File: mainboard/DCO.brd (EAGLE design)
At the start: 59.4 x 23 mm, 45 parts, among them IC101 LF353D, IC201 LF353D, P101 TRIMPOT 100K, U1 XMEGA-A4VQFN

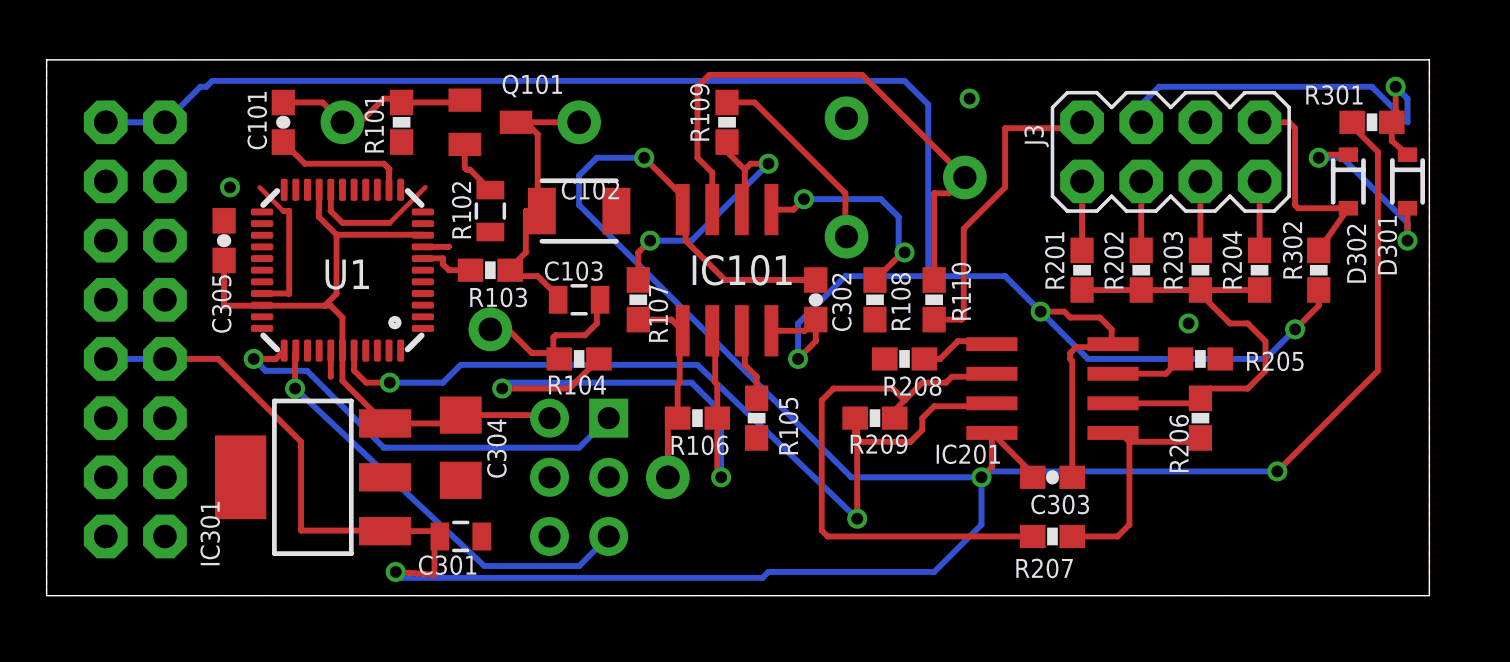
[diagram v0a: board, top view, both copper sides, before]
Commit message: rerouted, switched to TQFP xmega
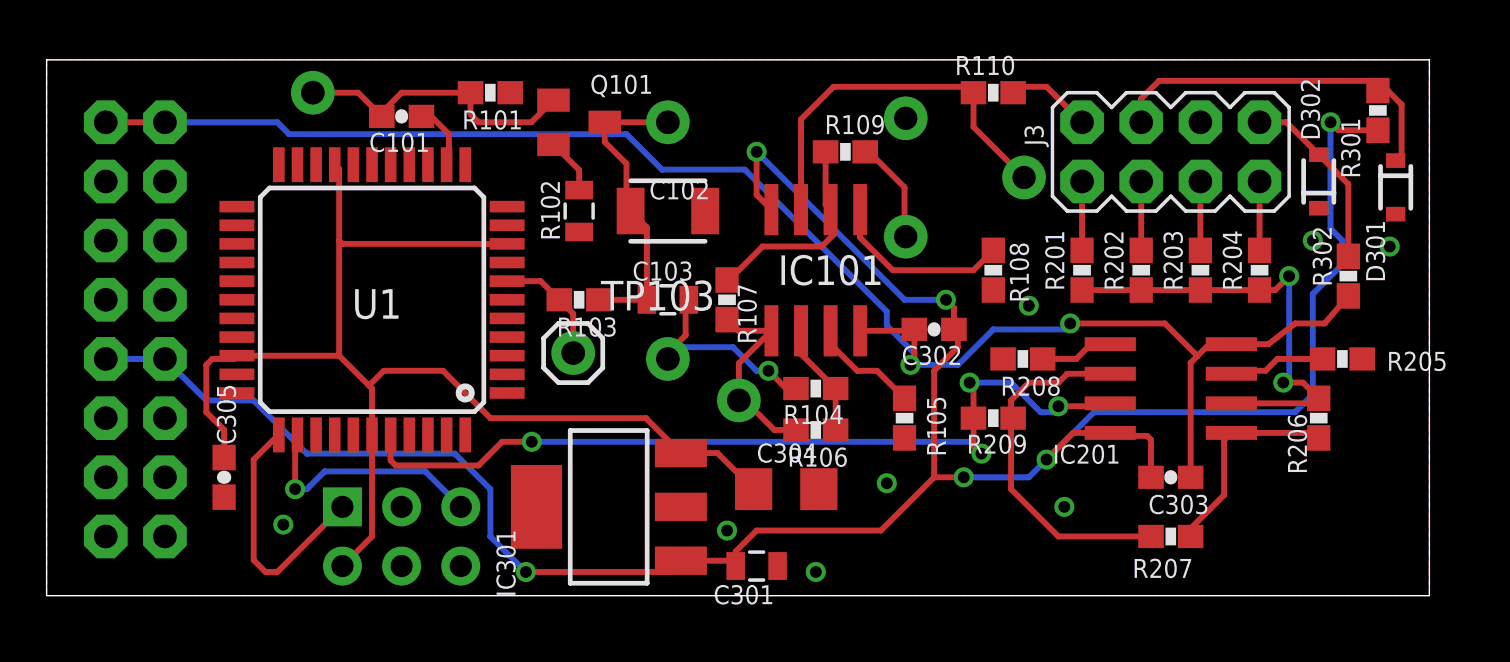
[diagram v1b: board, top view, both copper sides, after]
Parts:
- added TP105: (no value), SparkFun:1X01
- R102: value 3.9 -> 1
- U1: value XMEGA-A4VQFN -> XMEGA-A4TQFP; device custom:QFN44 -> avr-7:TQFP44
- moved C304 14.1 mm to (31.8, 4.57), turned to 0 degrees
- moved C301 12.8 mm to (30.5, 1.27)
- moved IC301 12.8 mm to (24.1, 3.81)
- moved R104 10.2 mm to (33.0, 8.89)
- moved C305 10.2 mm to (7.62, 5.08), turned to 90 degrees
- moved R110 9.25 mm to (40.6, 21.6), turned to 0 degrees
- moved H1 8.03 mm to (15.2, 2.54), turned to 270 degrees
- moved R105 6.35 mm to (36.8, 7.62)
- moved R205 6.10 mm to (55.6, 10.2)
- moved C302 5.24 mm to (38.1, 11.4), turned to 0 degrees
- moved R108 5.24 mm to (40.6, 14.0)
- moved R109 5.24 mm to (34.3, 19.1), turned to 0 degrees
- moved R106 5.11 mm to (33.0, 7.11)
- moved C101 5.09 mm to (15.2, 20.6), turned to 0 degrees
- moved TP104 5.08 mm to (26.7, 10.2)
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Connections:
- net FREQCV: now also TP103.1
- net N$13: now also TP105.1; no longer TP104.1
- net N$5: now also TP104.1; no longer TP103.1
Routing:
- net +3V3: track 29.0 -> 54.7 mm
- net GND: track 22.8 -> 0.00 mm, vias 5 -> 8
- net +12V: track 123.5 -> 103.5 mm, vias 4 -> 6
- net R104: track 23.9 -> 4.87 mm, vias 2 -> 0
- net -12V: track 87.5 -> 70.2 mm, vias 3 -> 2
- net OUT: track 13.6 -> 3.70 mm
- net N$19: track 23.9 -> 15.5 mm
- net RESET: track 18.6 -> 10.4 mm
- net N$11: track 24.4 -> 16.5 mm
- net PDI_DATA: track 18.8 -> 11.0 mm, vias 1 -> 0
- net N$12: track 8.58 -> 4.46 mm
- net N$2: track 8.67 -> 12.7 mm
- net N$3: track 12.7 -> 9.07 mm, vias 2 -> 0
- net FREQ: track 5.96 -> 2.85 mm
- net FREQCV: track 2.41 -> 5.10 mm
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
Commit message: edited labels
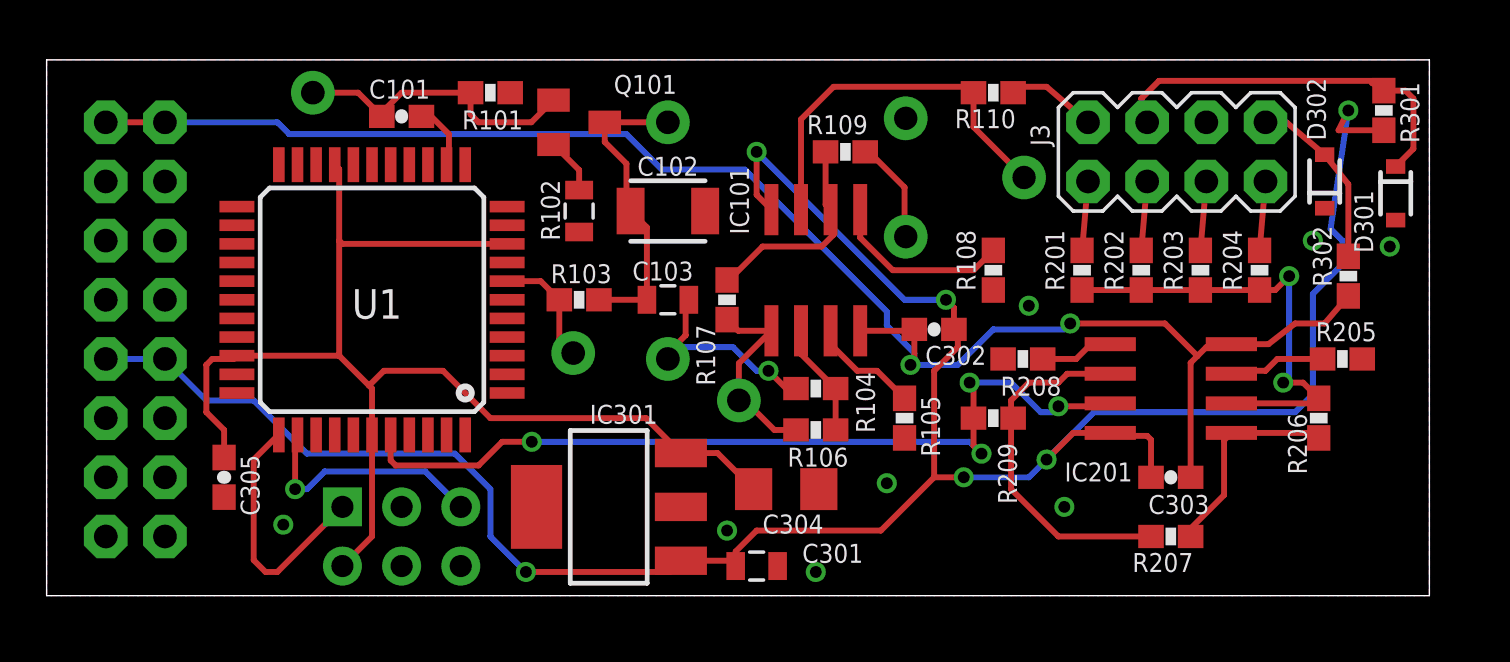
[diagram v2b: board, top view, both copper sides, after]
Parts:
- moved U$1 40.7 mm to (15.0, 15.2)
- moved J3 0.25 mm to (48.5, 19.1)
- moved R301 0.25 mm to (57.4, 20.8)
- moved D301 0.25 mm to (57.9, 17.3)
- moved D302 0.25 mm to (54.9, 17.8)
- flipped TP103 to the bottom
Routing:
- net +12V: track 103.5 -> 104.8 mm
- net +5V: track 15.5 -> 16.6 mm
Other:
- board text added: "Alpha 2"
- board text removed: "Alpha"

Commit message: Fixed design flaw - these resistors should be 10K
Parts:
- R301, R302: value 100K -> 10K
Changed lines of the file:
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@@
 <setting verticaltext="up"/>
 </settings>
-<grid distance="0.01" unitdist="inch" unit="inch" style="lines" multiple="1" display="yes" altdistance="0.005" altunitdist="inch" altunit="inch"/>
+<grid distance="0.05" unitdist="inch" unit="inch" style="lines" multiple="1" display="yes" altdistance="0.005" altunitdist="inch" altunit="inch"/>
 <layers>
-<layer number="1" name="Top" color="4" fill="1" visible="no" active="yes"/>
-<layer number="16" name="Bottom" color="1" fill="1" visible="no" active="yes"/>
+<layer number="1" name="Top" color="4" fill="1" visible="yes" active="yes"/>
+<layer number="16" name="Bottom" color="1" fill="1" visible="yes" active="yes"/>
 <layer number="17" name="Pads" color="2" fill="1" visible="yes" active="yes"/>
 <layer number="18" name="Vias" color="2" fill="1" visible="yes" active="yes"/>
 <layer number="19" name="Unrouted" color="16" fill="0" visible="yes" active="yes"/>
 <layer number="20" name="Dimension" color="15" fill="1" visible="yes" active="yes"/>
-<layer number="21" name="tPlace" color="6" fill="1" visible="no" active="yes"/>
+<layer number="21" name="tPlace" color="16" fill="1" visible="yes" active="yes"/>
 <layer number="22" name="bPlace" color="14" fill="1" visible="yes" active="yes"/>
-<layer number="23" name="tOrigins" color="15" fill="1" visible="no" active="yes"/>
+<layer number="23" name="tOrigins" color="15" fill="1" visible="yes" active="yes"/>
 <layer number="24" name="bOrigins" color="15" fill="1" visible="yes" active="yes"/>
 <layer number="25" name="tNames" color="7" fill="1" visible="no" active="yes"/>
-<layer number="26" name="bNames" color="7" fill="1" visible="yes" active="yes"/>
+<layer number="26" name="bNames" color="7" fill="1" visible="no" active="yes"/>
 <layer number="27" name="tValues" color="7" fill="1" visible="no" active="yes"/>
 <layer number="28" name="bValues" color="7" fill="1" visible="no" active="yes"/>
@@
 <layer number="49" name="Reference" color="7" fill="1" visible="no" active="yes"/>
 <layer number="50" name="dxf" color="7" fill="1" visible="no" active="no"/>
-<layer number="51" name="tDocu" color="6" fill="1" visible="no" active="yes"/>
-<layer number="52" name="bDocu" color="7" fill="1" visible="yes" active="yes"/>
+<layer number="51" name="tDocu" color="6" fill="1" visible="yes" active="yes"/>
+<layer number="52" name="bDocu" color="7" fill="1" visible="no" active="yes"/>
 <layer number="53" name="tGND_GNDA" color="7" fill="9" visible="no" active="no"/>
 <layer number="54" name="bGND_GNDA" color="1" fill="9" visible="no" active="no"/>
@@
 <attribute name="VALUE" x="56.261" y="16.764" size="0.4064" layer="27" rot="R90"/>
 </element>
-<element name="R301" library="SparkFun" package="0603-RES" value="100K" x="57.404" y="20.828" smashed="yes" rot="R90">
+<element name="R301" library="SparkFun" package="0603-RES" value="10K" x="57.404" y="20.828" smashed="yes" rot="R90">
 <attribute name="NAME" x="58.928" y="19.431" size="0.8128" layer="25" font="vector" rot="R90"/>
 <attribute name="VALUE" x="58.547" y="19.812" size="0.4064" layer="27" font="vector" rot="R90"/>
 </element>
-<element name="R302" library="SparkFun" package="0603-RES" value="100K" x="55.88" y="13.716" smashed="yes" rot="R270">
+<element name="R302" library="SparkFun" package="0603-RES" value="10K" x="55.88" y="13.716" smashed="yes" rot="R270">
 <attribute name="NAME" x="54.356" y="15.875" size="0.8128" layer="25" font="vector" rot="R270"/>
 <attribute name="VALUE" x="54.737" y="14.732" size="0.4064" layer="27" font="vector" rot="R270"/>

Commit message: Fix for design flaw - fine pitch control was attached backwards.
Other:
- board text added: "Alpha 3"
- board text removed: "Alpha 2"
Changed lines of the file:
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@@
 <text x="58.42" y="6.35" size="1.6764" layer="22" font="vector" ratio="15" rot="MR0">Controlled</text>
 <text x="58.42" y="4.318" size="1.6764" layer="22" font="vector" ratio="15" rot="MR0">Oscillator</text>
-<text x="58.42" y="2.286" size="1.6764" layer="22" font="vector" ratio="15" rot="MR0">Alpha 2</text>
+<text x="58.42" y="2.286" size="1.6764" layer="22" font="vector" ratio="15" rot="MR0">Alpha 3</text>
 <text x="47.498" y="13.208" size="1.27" layer="22" font="vector" ratio="15" rot="MR0">Output Gain Adj.</text>
 <wire x1="10.16" y1="3.048" x2="11.43" y2="3.556" width="0.254" layer="22"/>
